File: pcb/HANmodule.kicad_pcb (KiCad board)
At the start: 2 copper layers, 62 x 46 mm, 32 parts, among them J1 HAN port, J2 Debug, J3 Prog, SW1 Reset, U1 RT9013-3.3v, U2 ESP-12F

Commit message: Updated schematic
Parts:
- C1: footprint Capacitor_THT:CP_Radial_D10.0mm_P5.00mm -> Capacitor_THT:CP_Radial_D22.0mm_P10.00mm_SnapIn
- moved C1 14.3 mm to (119.0, 70.0)
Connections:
- J2 pad 1: Net-(J2-Pad1) -> /DB_TX

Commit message: PCB rev 1
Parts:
- removed D3: Meter data, LED_THT:LED_D3.0mm
- removed D4: Wifi, LED_THT:LED_D3.0mm
- removed D5: MQTT, LED_THT:LED_D3.0mm
- removed D6: Fault, LED_THT:LED_D3.0mm
- removed R3: 100k, Resistor_SMD:R_0603_1608Metric_Pad1.05x0.95mm_HandSolder
- added C8: 10uF, Capacitor_SMD:C_0603_1608Metric_Pad1.05x0.95mm_HandSolder, F.Cu at (137.6, 73.0)
- added C9: 100n, Capacitor_SMD:C_0603_1608Metric_Pad1.05x0.95mm_HandSolder, F.Cu at (137.6, 75.0)
- added Q1: SI2301DS_P-FET, Package_TO_SOT_SMD:SOT-23_Handsoldering, F.Cu at (100.5, 48.0)
- added Q2: BSS139, Package_TO_SOT_SMD:SOT-23_Handsoldering, F.Cu at (110.5, 59.0)
- added R14: 34k, Resistor_SMD:R_0603_1608Metric_Pad1.05x0.95mm_HandSolder, F.Cu at (131.9, 65.0)
- added R15: 100k, Resistor_SMD:R_0603_1608Metric_Pad1.05x0.95mm_HandSolder, F.Cu at (131.9, 73.0)
- added REF**: ESD-Logo_6.6x6mm_SilkScreen, Symbol:ESD-Logo_6.6x6mm_SilkScreen, B.Cu at (145.5, 60.5)
- added REF**: ESD-Logo_6.6x6mm_SilkScreen, Symbol:ESD-Logo_6.6x6mm_SilkScreen, F.Cu at (131.5, 78.0)
- added U3: ESP-12F, RF_Module:ESP-12E, F.Cu at (145.0, 58.0)
- C1: value CP -> 1uF; footprint Capacitor_THT:CP_Radial_D22.0mm_P10.00mm_SnapIn -> Capacitor_SMD:C_0603_1608Metric_Pad1.05x0.95mm_HandSolder
- C2: value CP -> 0.1F 5.5V FC0H104ZFTBR24; footprint Capacitor_THT:CP_Radial_D10.0mm_P5.00mm -> Capacitor_SMD:CP_Elec_10x10.5
- C4: value 1uF -> 1n
- C6: value 10uF -> 1,75u
- D1: value D_Schottky -> Heartbeat; footprint Diode_SMD:D_SMA-SMB_Universal_Handsoldering -> LED_SMD:LED_0805_2012Metric_Pad1.15x1.40mm_HandSolder
- D2: value Heartbeat -> Fault; footprint LED_THT:LED_D3.0mm -> LED_SMD:LED_0805_2012Metric_Pad1.15x1.40mm_HandSolder
- J1: value HAN port -> M20-7920342R; footprint Connector_PinSocket_2.54mm:PinSocket_2x03_P2.54mm_Horizontal -> SamacSys_Parts:M20-7920342R
- J2: footprint Connector_PinHeader_2.54mm:PinHeader_1x02_P2.54mm_Vertical -> Connector_PinHeader_2.54mm:PinHeader_1x02_P2.54mm_Horizontal
- J3: footprint Connector_PinSocket_2.54mm:PinSocket_1x06_P2.54mm_Vertical -> Connector_PinHeader_2.54mm:PinHeader_1x06_P2.54mm_Horizontal
- R12: value 1k -> 100k
- R13: value 1k -> 102k
- R2: value 1k -> 55R
- R5: value 1k -> 113k
- R6: value 1k -> 13k3
- SW1: footprint Button_Switch_SMD:Panasonic_EVQPUJ_EVQPUA -> Button_Switch_SMD:Panasonic_EVQPUM_EVQPUD
- U1: value RT9013-3.3v -> TLV75530PDBV | RT9013
- U2: value ESP-12F -> NCP308SNADJT1G; footprint RF_Module:ESP-12E -> Package_SO:TSOP-6_1.65x3.05mm_P0.95mm
- moved R9 46.1 mm to (152.6, 75.0), turned to 180 degrees
- moved J2 36.1 mm to (129.5, 55.5), turned to 90 degrees
- moved R13 34.5 mm to (131.9, 63.0), turned to 180 degrees
- moved U2 32.9 mm to (117.0, 73.0)
- moved R12 27.8 mm to (131.9, 61.0), turned to 180 degrees
- moved C5 26.3 mm to (116.9, 70.0), turned to 0 degrees
- moved C2 23.9 mm to (120.0, 60.0), turned to 90 degrees
- moved R5 23.4 mm to (121.0, 71.1), turned to 270 degrees
- moved R6 21.0 mm to (121.0, 74.9), turned to 270 degrees
- moved D1 19.6 mm to (123.5, 47.9), turned to 180 degrees
- moved C6 17.4 mm to (117.1, 76.0), turned to 180 degrees
- moved C4 17.3 mm to (123.0, 74.9), turned to 270 degrees
- moved U1 17.1 mm to (120.0, 83.0)
- moved R2 16.1 mm to (110.1, 55.0), turned to 180 degrees
- moved J3 15.6 mm to (153.1, 80.5), turned to 270 degrees
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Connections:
- C1 pad 1: Net-(C1-Pad1) -> +4V
- C1 pad 2: Net-(C1-Pad2) -> GND
- C2 pad 1: Net-(C1-Pad2) -> +4V
- C3 pad 1: Net-(C1-Pad1) -> +3V0
- C4 pad 1: +3V3 -> Net-(C4-Pad1)
- C5 pad 2: /~RST -> +4V
- C6 pad 1: +3V3 -> Net-(C6-Pad1)
- C7 pad 1: +3V3 -> GND
- C7 pad 2: GND -> /~RST
- D1 pad 1: Net-(C1-Pad1) -> /~LED
- D1 pad 2: VCC -> Net-(D1-Pad2)
- D2 pad 1: /GPIO0 -> /~FAULT_LED
- J1 pad 1: Net-(J1-Pad1) -> (no net)
- J1 pad 2: /DIN -> (no net)
- J1 pad 3: VCC -> (no net)
- J1 pad 4: GND -> /DOUT
- J1 pad 5: /DOUT -> VCC
- J1 pad 6: Net-(J1-Pad6) -> GND
- J3 pad 1: Net-(J3-Pad1) -> /GPIO0
- J3 pad 2: Net-(J3-Pad2) -> /TX
- J3 pad 3: Net-(J3-Pad3) -> /RX
- J3 pad 4: Net-(J3-Pad4) -> +3V0
- J3 pad 5: Net-(J3-Pad5) -> /~RST
- J3 pad 6: Net-(J3-Pad6) -> GND
- R1 pad 1: +3V3 -> +3V0
- R1 pad 2: Net-(D2-Pad2) -> Net-(D1-Pad2)
- R10 pad 1: /GPIO0 -> /GPIO2
- R10 pad 2: +3V3 -> +3V0
- R11 pad 1: /GPIO2 -> +3V0
- R11 pad 2: +3V3 -> /EN
- R13 pad 1: /DIN -> Net-(R13-Pad1)
- R13 pad 2: Net-(R13-Pad2) -> +4V
- R2 pad 1: +3V3 -> +4V
- R4 pad 1: +3V3 -> +3V0
- R4 pad 2: Net-(D4-Pad2) -> Net-(D2-Pad2)
- R5 pad 1: +3V3 -> +4V
- R5 pad 2: Net-(D5-Pad2) -> Net-(C4-Pad1)
- R6 pad 1: +3V3 -> Net-(C4-Pad1)
- R6 pad 2: Net-(D6-Pad2) -> GND
- R8 pad 1: /EN -> /~RST
- R8 pad 2: +3V3 -> +3V0
- R9 pad 1: /~RST -> /GPIO0
- R9 pad 2: +3V3 -> +3V0
- U1 pad 1: Net-(C1-Pad1) -> +4V
- U1 pad 3: Net-(C1-Pad1) -> +4V
- U1 pad 4: Net-(U1-Pad4) -> (no net)
- U1 pad 5: +3V3 -> +3V0
- U2 pad 1: /RST -> /EN
- U2 pad 2: Net-(U2-Pad2) -> GND
- U2 pad 3: /EN -> (no net)
- U2 pad 4: Net-(U2-Pad4) -> Net-(C6-Pad1)
- U2 pad 5: /FAULT_LED -> Net-(C4-Pad1)
- U2 pad 6: /MQTT_LED -> +4V
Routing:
- net +3V0: track 0.00 -> 98.9 mm, vias 0 -> 2
- net /~RST: track 0.00 -> 78.1 mm
- net +4V: track 0.00 -> 65.4 mm
- net /DOUT: track 0.00 -> 47.3 mm, vias 0 -> 2
- net /EN: track 0.00 -> 46.8 mm, vias 0 -> 3
- net /~FAULT_LED: track 0.00 -> 39.9 mm, vias 0 -> 2
- net /GPIO2: track 0.00 -> 34.3 mm, vias 0 -> 2
- net /~LED: track 0.00 -> 33.6 mm, vias 0 -> 2
- net /TX: track 0.00 -> 30.7 mm, vias 0 -> 1
- net /RX: track 0.00 -> 28.9 mm, vias 0 -> 1
- net /GPIO0: track 0.00 -> 20.9 mm
- net Net-(Q1-Pad2): track 0.00 -> 15.9 mm
- net /GPIO15: track 0.00 -> 12.3 mm
- net Net-(R13-Pad1): track 0.00 -> 10.9 mm
- net GND: track 0.00 -> 8.95 mm, vias 0 -> 100
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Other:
- outline, holes or cut-outs redrawn
- rule trace_min: 0.2 -> 0.14
- board text added: "DTR"
- board text added: "Debug"
- board text added: "Fault"
- board text added: "GND"
- board text added: "Heartbeat"
- board text added: "Kamstrup Radius interface module"
- board text added: "RTS"
- board text added: "RX"
- board text added: "Reset"
- board text added: "Rev 1"
- board text added: "TX"
- board text added: "VCC"
- board text added: "https://github.com/Asbjoern /Kamstrup-Radius-Interface"

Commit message: PCB rev2 to be tested
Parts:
- removed REF** (x2): ESD-Logo_6.6x6mm_SilkScreen, Symbol:ESD-Logo_6.6x6mm_SilkScreen
- added L1: 2.2UH 4x4mm, Inductor_SMD:L_Bourns-SRN4018, F.Cu at (132.7, 79.0)
- added R16: 1k, Resistor_SMD:R_0603_1608Metric_Pad1.05x0.95mm_HandSolder, F.Cu at (108.1, 55.8)
- added R17: 2k7, Resistor_SMD:R_0603_1608Metric_Pad1.05x0.95mm_HandSolder, F.Cu at (108.1, 54.0)
- added R18: 330k, Resistor_SMD:R_0603_1608Metric_Pad1.05x0.95mm_HandSolder, F.Cu at (131.2, 88.2)
- added R19: 100k, Resistor_SMD:R_0603_1608Metric_Pad1.05x0.95mm_HandSolder, F.Cu at (131.2, 86.8)
- added R20: 100k, Resistor_SMD:R_0603_1608Metric_Pad1.05x0.95mm_HandSolder, F.Cu at (146.5, 74.8)
- added R3: NC, Resistor_SMD:R_0603_1608Metric_Pad1.05x0.95mm_HandSolder, F.Cu at (108.0, 59.4)
- C1: value 1uF -> 4.7uF
- C3: value 1uF -> 10uF
- Q1: footprint Package_TO_SOT_SMD:SOT-23_Handsoldering -> Package_TO_SOT_SMD:SOT-23
- Q2: value BSS139 -> BC807; footprint Package_TO_SOT_SMD:SOT-23_Handsoldering -> Package_TO_SOT_SMD:SOT-23
- R2: value 55R -> 4k7
- U1: value TLV75530PDBV | RT9013 -> TLV62568DBV; footprint Package_TO_SOT_SMD:SOT-23-5_HandSoldering -> Package_TO_SOT_SMD:SOT-23-5
- moved C1 12.5 mm to (128.5, 83.6)
- moved U1 11.4 mm to (131.4, 84.0), turned to 180 degrees
- moved C3 10.3 mm to (134.2, 83.6)
- moved R2 3.31 mm to (108.1, 57.6)
- moved Q2 2.60 mm to (111.8, 56.8), turned to 0 degrees
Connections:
- J1 pad 3: (no net) -> /DIN
- Q2 pad 1: /EN -> Net-(Q2-Pad1)
- Q2 pad 2: +4V -> Net-(Q2-Pad2)
- Q2 pad 3: Net-(Q1-Pad2) -> +4V
- R2 pad 1: +4V -> Net-(Q2-Pad2)
- U1 pad 3: +4V -> Net-(L1-Pad1)
- U1 pad 4: (no net) -> +4V
- U1 pad 5: +3V0 -> Net-(R18-Pad2)
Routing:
- net /DIN: track 0.00 -> 61.9 mm, vias 0 -> 2
- net /EN: track 46.8 -> 35.9 mm, vias 3 -> 2
- net /DOUT: track 47.3 -> 42.5 mm
- net Net-(L1-Pad1): track 0.00 -> 4.48 mm
- net Net-(Q2-Pad2): track 0.00 -> 3.88 mm
- net Net-(Q2-Pad1): track 0.00 -> 3.67 mm
- net +3V0: track 98.9 -> 95.8 mm, vias 2 -> 4
- net Net-(R18-Pad2): track 0.00 -> 3.05 mm
- net /GPIO15: track 12.3 -> 14.2 mm
- net GND: track 8.95 -> 7.87 mm, vias 100 -> 99
- net Net-(Q1-Pad2): track 15.9 -> 15.2 mm
- net VCC: track 4.79 -> 5.29 mm
- net +4V: track 65.4 -> 65.5 mm, vias 0 -> 6
- added copper zone on B.Cu, net +4V
- added copper zone on F.Cu, net +4V
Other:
- board text added: "Rev 2"
- board text removed: "Rev 1"

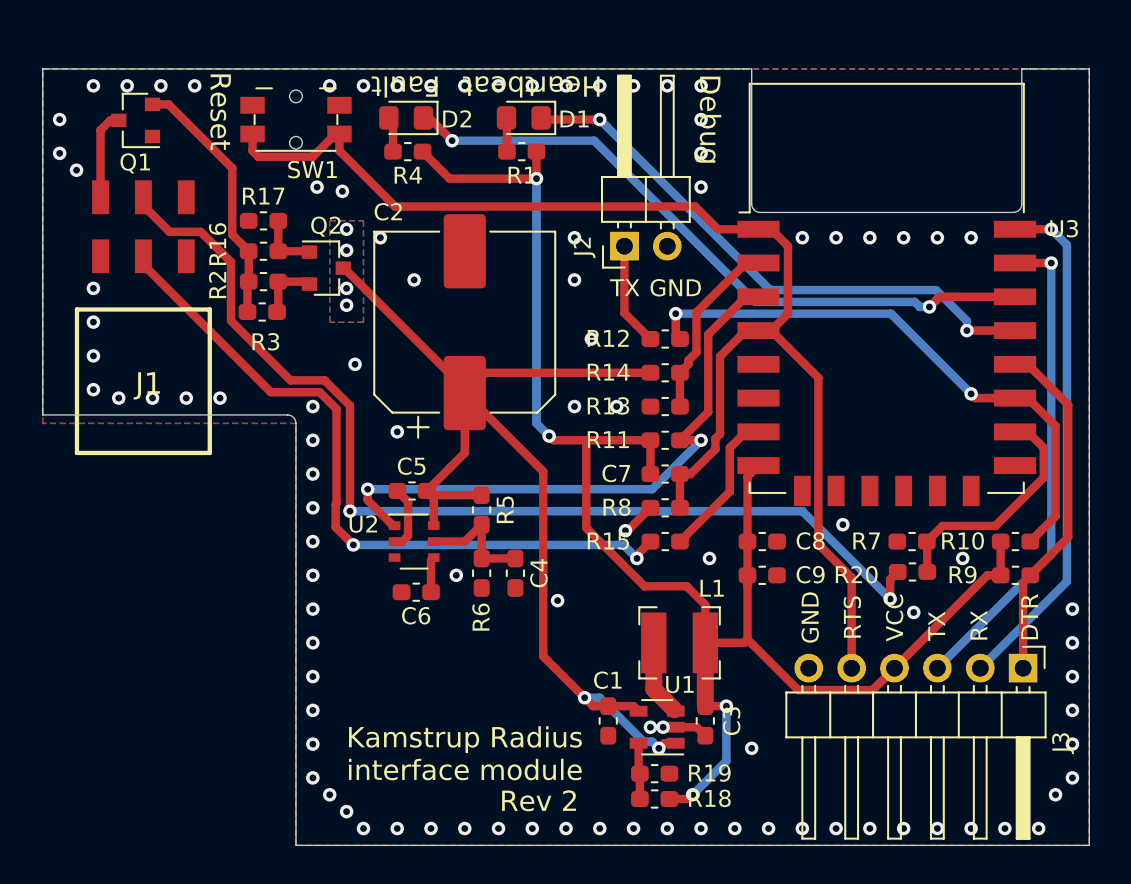
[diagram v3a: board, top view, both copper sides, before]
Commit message: Improved power design
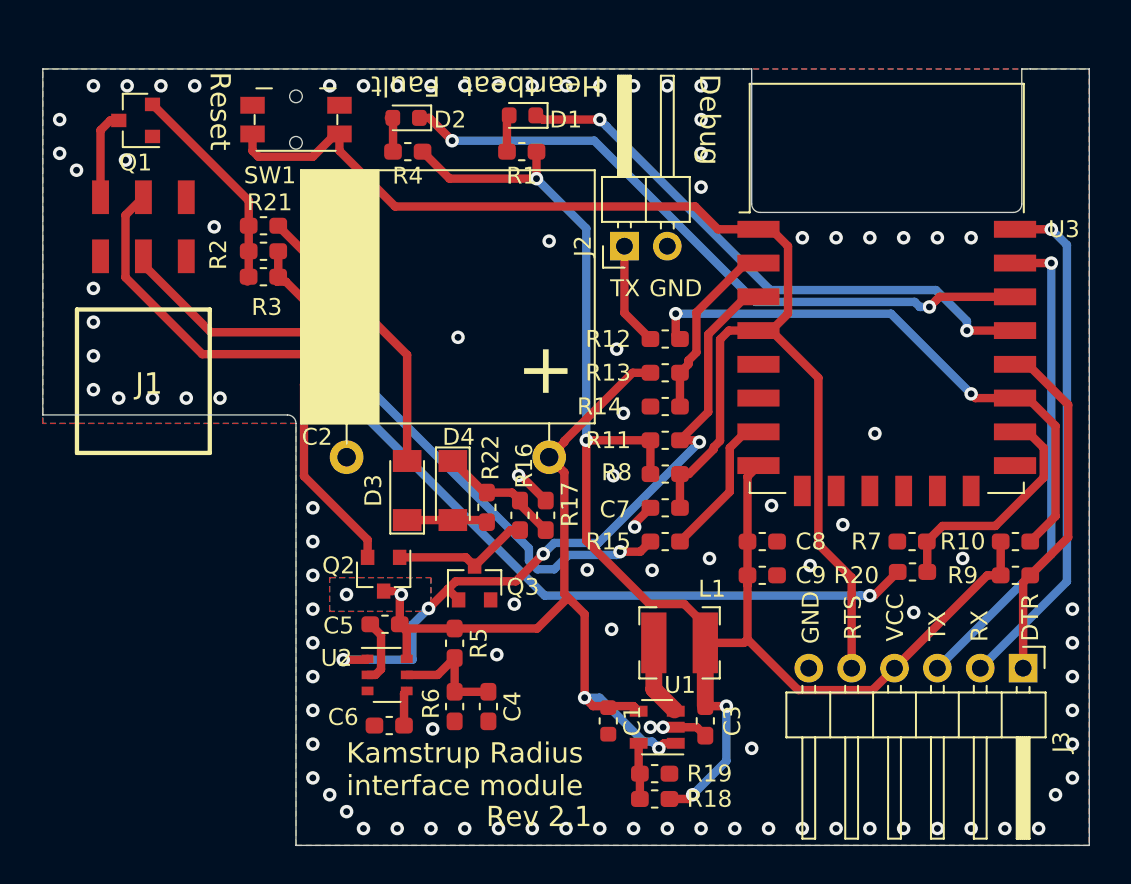
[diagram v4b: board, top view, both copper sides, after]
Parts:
- added D3: LL4148, Diode_SMD:D_MiniMELF, F.Cu at (116.6, 70.0)
- added D4: LL4148, Diode_SMD:D_MiniMELF, F.Cu at (119.3, 70.0)
- added Q3: SI2302DS/2N7002, Package_TO_SOT_SMD:SOT-23, F.Cu at (120.6, 75.5)
- added R21: 0R, Resistor_SMD:R_0603_1608Metric_Pad1.05x0.95mm_HandSolder, F.Cu at (108.1, 54.3)
- added R22: NC, Resistor_SMD:R_0603_1608Metric_Pad1.05x0.95mm_HandSolder, F.Cu at (121.3, 71.0)
- C1: footprint Capacitor_SMD:C_0603_1608Metric_Pad1.05x0.95mm_HandSolder -> Capacitor_SMD:C_0603_1608Metric
- C2: value 0.1F 5.5V FC0H104ZFTBR24 -> 0.47F; footprint Capacitor_SMD:CP_Elec_10x10.5 -> housings:c_sup 17,3x15x8.5P12
- C6: value 1,75u -> 1.5u
- D1, D2: footprint LED_SMD:LED_0805_2012Metric_Pad1.15x1.40mm_HandSolder -> LED_SMD:LED_0603_1608Metric
- Q2: value BC807 -> SI2301DS_P-FET
- R13: value 102k -> 100k
- R14: value 34k -> 33k
- R16: value 1k -> 10k
- R17: value 2k7 -> 4k3
- R2: value 4k7 -> 4R7
- R3: value NC -> 5R6
- R5: value 113k -> 110k
- R6: value 13k3 -> 16k
- moved R17 24.2 mm to (124.8, 71.4), turned to 270 degrees
- moved R16 21.8 mm to (123.3, 71.4), turned to 270 degrees
- moved Q2 18.5 mm to (115.2, 74.9), turned to 270 degrees
- moved C4 8.06 mm to (121.4, 82.8)
- moved C5 8.06 mm to (115.3, 77.9)
- moved C6 8.06 mm to (115.5, 83.9)
- moved R5 8.06 mm to (119.4, 79.0)
- moved R6 8.06 mm to (119.4, 82.8)
- moved U2 8.06 mm to (115.4, 80.9)
- moved C2 6.08 mm to (119.0, 66.0), turned to 0 degrees
- moved R3 2.09 mm to (108.1, 57.3)
- moved R2 1.80 mm to (108.1, 55.8)
- moved D1 0.17 mm to (123.4, 47.8)
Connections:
- R16 pad 1: Net-(Q2-Pad1) -> Net-(D4-Pad1)
- R16 pad 2: Net-(Q1-Pad2) -> Net-(Q2-Pad1)
- R17 pad 2: Net-(Q2-Pad1) -> Net-(D4-Pad1)
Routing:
- net Net-(Q2-Pad2): track 3.88 -> 21.8 mm
- net Net-(D3-Pad2): track 0.00 -> 17.1 mm
- net +4V: track 65.5 -> 49.0 mm, vias 6 -> 4
- net Net-(D4-Pad1): track 0.00 -> 7.54 mm
- net /EN: track 35.9 -> 42.1 mm, vias 2 -> 4
- net Net-(D3-Pad1): track 0.00 -> 4.78 mm
- net Net-(Q2-Pad1): track 3.67 -> 8.22 mm
- net /DOUT: track 42.5 -> 39.1 mm
- net Net-(Q1-Pad2): track 15.2 -> 12.8 mm
- net /DIN: track 61.9 -> 59.7 mm
- net GND: track 7.87 -> 9.57 mm, vias 99 -> 102
- net +3V0: track 95.8 -> 94.4 mm
- net /~RST: track 78.1 -> 78.7 mm
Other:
- board text added: "Rev 2.1"
